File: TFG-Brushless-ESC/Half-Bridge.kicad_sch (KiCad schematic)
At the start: 9 parts, among them Q5 IRF1310, Q6 IRF1310, U5 IR2101

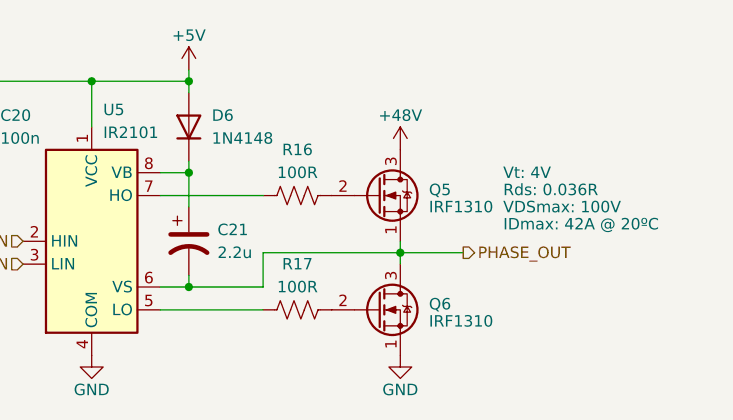
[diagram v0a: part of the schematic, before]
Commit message: Changes in half-bridge
Corrected voltage from 48 to 24V and 5V Vcc to 12V Vcc
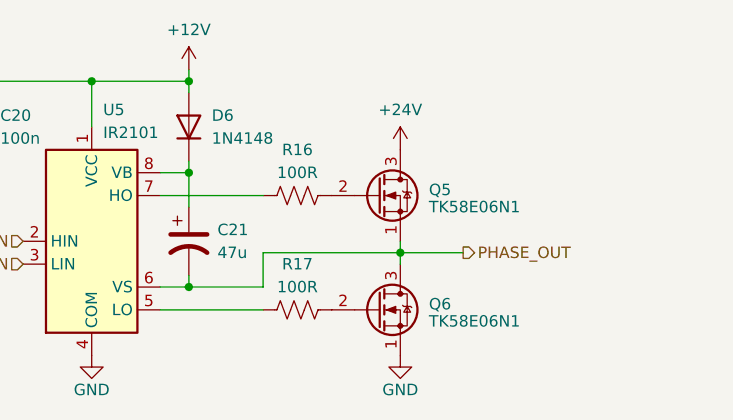
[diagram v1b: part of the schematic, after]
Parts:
- C21: value 2.2u -> 47u
- Q5, Q6: value IRF1310 -> TK58E06N1
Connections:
- net +48V renamed +24V
- net +5V renamed +12V
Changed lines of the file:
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@@
 		)
 		(instances
-			(project "RTSpeed"
+			(project "TFG-Brushless-ESC"
 				(path "/fc8dd9a9-f99a-4338-8182-2c8b4b8ed6dd/b5458e57-2ddd-4d30-9620-d640c1a391c8"
 					(reference "#PWR042")
@@
 		)
 		(instances
-			(project "RTSpeed"
+			(project "TFG-Brushless-ESC"
 				(path "/fc8dd9a9-f99a-4338-8182-2c8b4b8ed6dd/b5458e57-2ddd-4d30-9620-d640c1a391c8"
 					(reference "C22")
@@
 		)
 		(instances
-			(project "RTSpeed"
+			(project "TFG-Brushless-ESC"
 				(path "/fc8dd9a9-f99a-4338-8182-2c8b4b8ed6dd/211b6883-96c8-42a2-bec5-a4dfd4e56ba6"
 					(reference "R17")
@@
 				(path "/fc8dd9a9-f99a-4338-8182-2c8b4b8ed6dd/f6e668ab-a50d-4861-bee8-58a57ed6fcc7"
 					(reference "R15")
+					(unit 1)
+				)
+			)
+		)
+	)
+	(symbol
+		(lib_id "power:+24V")
+		(at 96.52 78.105 0)
+		(unit 1)
+		(exclude_from_sim no)
+		(in_bom yes)
+		(on_board yes)
+		(dnp no)
+		(fields_autoplaced yes)
+		(property "Reference" "#PWR041"
+			(at 96.52 81.915 0)
+			(effects
+				(font
+					(size 1.27 1.27)
+				)
+				(hide yes)
+			)
+		)
+		(property "Value" "+24V"
+			(at 96.52 73.66 0)
+			(effects
+				(font
+					(size 1.27 1.27)
+				)
+			)
+		)
+		(property "Footprint" ""
+			(at 96.52 78.105 0)
+			(effects
+				(font
+					(size 1.27 1.27)
+				)
+				(hide yes)
+			)
+		)
+		(property "Datasheet" ""
+			(at 96.52 78.105 0)
+			(effects
+				(font
+					(size 1.27 1.27)
+				)
+				(hide yes)
+			)
+		)
+		(property "Description" "Power symbol creates a global label with name \"+24V\""
+			(at 96.52 78.105 0)
+			(effects
+				(font
+					(size 1.27 1.27)
+				)
+				(hide yes)
+			)
+		)
+		(pin "1"
+		)
+		(instances
+			(project "TFG-Brushless-ESC"
+				(path "/fc8dd9a9-f99a-4338-8182-2c8b4b8ed6dd/b5458e57-2ddd-4d30-9620-d640c1a391c8"
+					(reference "#PWR041")
+					(unit 1)
+				)
+				(path "/fc8dd9a9-f99a-4338-8182-2c8b4b8ed6dd/f6e668ab-a50d-4861-bee8-58a57ed6fcc7"
+					(reference "#PWR046")
+					(unit 1)
+				)
+				(path "/fc8dd9a9-f99a-4338-8182-2c8b4b8ed6dd/211b6883-96c8-42a2-bec5-a4dfd4e56ba6"
+					(reference "#PWR051")
 					(unit 1)
 				)
@@
 			)
 		)
-		(property "Value" "IRF1310"
+		(property "Value" "TK58E06N1"
 			(at 99.695 84.455 0)
 			(effects
@@
 				)
 				(justify left)
+				(hide yes)
 			)
 		)
@@
 				)
 				(justify left)
+				(hide yes)
 			)
 		)
@@
 				)
 				(justify left)
+				(hide yes)
 			)
 		)
@@
 				)
 				(justify left)
+				(hide yes)
 			)
 		)
@@
 		)
 		(instances
-			(project "RTSpeed"
+			(project "TFG-Brushless-ESC"
 				(path "/fc8dd9a9-f99a-4338-8182-2c8b4b8ed6dd/211b6883-96c8-42a2-bec5-a4dfd4e56ba6"
 					(reference "Q5")
@@
 		)
 		(instances
-			(project "RTSpeed"
+			(project "TFG-Brushless-ESC"
 				(path "/fc8dd9a9-f99a-4338-8182-2c8b4b8ed6dd/211b6883-96c8-42a2-bec5-a4dfd4e56ba6"
 					(reference "D6")
@@
 		)
 		(instances
-			(project "RTSpeed"
+			(project "TFG-Brushless-ESC"
 				(path "/fc8dd9a9-f99a-4338-8182-2c8b4b8ed6dd/b5458e57-2ddd-4d30-9620-d640c1a391c8"
 					(reference "#PWR055")
@@
 		)
 		(instances
-			(project "RTSpeed"
+			(project "TFG-Brushless-ESC"
 				(path "/fc8dd9a9-f99a-4338-8182-2c8b4b8ed6dd/211b6883-96c8-42a2-bec5-a4dfd4e56ba6"
 					(reference "U5")
@@
 		)
 		(instances
-			(project "RTSpeed"
+			(project "TFG-Brushless-ESC"
 				(path "/fc8dd9a9-f99a-4338-8182-2c8b4b8ed6dd/b5458e57-2ddd-4d30-9620-d640c1a391c8"
 					(reference "#PWR044")
@@
 		)
 		(instances
-			(project "RTSpeed"
+			(project "TFG-Brushless-ESC"
 				(path "/fc8dd9a9-f99a-4338-8182-2c8b4b8ed6dd/211b6883-96c8-42a2-bec5-a4dfd4e56ba6"
 					(reference "R16")
@@
 		)
 		(instances
-			(project "RTSpeed"
+			(project "TFG-Brushless-ESC"
 				(path "/fc8dd9a9-f99a-4338-8182-2c8b4b8ed6dd/211b6883-96c8-42a2-bec5-a4dfd4e56ba6"
 					(reference "C20")
@@
 			)
 		)
-		(property "Value" "IRF1310"
+		(property "Value" "TK58E06N1"
 			(at 99.695 97.1549 0)
 			(effects
@@
 		)
 		(instances
-			(project "RTSpeed"
+			(project "TFG-Brushless-ESC"
 				(path "/fc8dd9a9-f99a-4338-8182-2c8b4b8ed6dd/211b6883-96c8-42a2-bec5-a4dfd4e56ba6"
 					(reference "Q6")
@@
 		)
 		(instances
-			(project "RTSpeed"
+			(project "TFG-Brushless-ESC"
 				(path "/fc8dd9a9-f99a-4338-8182-2c8b4b8ed6dd/b5458e57-2ddd-4d30-9620-d640c1a391c8"
 					(reference "#PWR043")
@@
 				(path "/fc8dd9a9-f99a-4338-8182-2c8b4b8ed6dd/211b6883-96c8-42a2-bec5-a4dfd4e56ba6"
 					(reference "#PWR053")
-					(unit 1)
-				)
-			)
-		)
-	)
-	(symbol
-		(lib_id "power:+48V")
-		(at 96.52 78.105 0)
-		(unit 1)
-		(exclude_from_sim no)
-		(in_bom yes)
-		(on_board yes)
-		(dnp no)
-		(property "Reference" "#PWR041"
-			(at 96.52 81.915 0)
-			(effects
-				(font
-					(size 1.27 1.27)
-				)
-				(hide yes)
-			)
-		)
-		(property "Value" "+48V"
-			(at 96.52 74.295 0)
-			(effects
-				(font
-					(size 1.27 1.27)
-				)
-			)
-		)
-		(property "Footprint" ""
-			(at 96.52 78.105 0)
-			(effects
-				(font
-					(size 1.27 1.27)
-				)
-				(hide yes)
-			)
-		)
-		(property "Datasheet" ""
-			(at 96.52 78.105 0)
-			(effects
-				(font
-					(size 1.27 1.27)
-				)
-				(hide yes)
-			)
-		)
-		(property "Description" ""
-			(at 96.52 78.105 0)
-			(effects
-				(font
-					(size 1.27 1.27)
-				)
-				(hide yes)
-			)
-		)
-		(pin "1"
-		)
-		(instances
-			(project "RTSpeed"
-				(path "/fc8dd9a9-f99a-4338-8182-2c8b4b8ed6dd/b5458e57-2ddd-4d30-9620-d640c1a391c8"
-					(reference "#PWR041")
-					(unit 1)
-				)
-				(path "/fc8dd9a9-f99a-4338-8182-2c8b4b8ed6dd/f6e668ab-a50d-4861-bee8-58a57ed6fcc7"
-					(reference "#PWR046")
-					(unit 1)
-				)
-				(path "/fc8dd9a9-f99a-4338-8182-2c8b4b8ed6dd/211b6883-96c8-42a2-bec5-a4dfd4e56ba6"
-					(reference "#PWR051")
 					(unit 1)
 				)
@@
 			)
 		)
-		(property "Value" "2.2u"
+		(property "Value" "47u"
 			(at 76.2 89.535 0)
 			(effects
@@
 		)
 		(instances
-			(project "RTSpeed"
+			(project "TFG-Brushless-ESC"
 				(path "/fc8dd9a9-f99a-4338-8182-2c8b4b8ed6dd/211b6883-96c8-42a2-bec5-a4dfd4e56ba6"
 					(reference "C21")
@@
 	)
 	(symbol
-		(lib_id "power:+5V")
+		(lib_id "power:+12V")
 		(at 73.025 69.215 0)
 		(unit 1)
@@
 		(on_board yes)
 		(dnp no)
+		(fields_autoplaced yes)
 		(property "Reference" "#PWR040"
 			(at 73.025 73.025 0)
@@
 			)
 		)
-		(property "Value" "+5V"
-			(at 73.025 65.405 0)
+		(property "Value" "+12V"
+			(at 73.025 64.77 0)
 			(effects
 				(font
@@
 			)
 		)
-		(property "Description" ""
+		(property "Description" "Power symbol creates a global label with name \"+12V\""
 			(at 73.025 69.215 0)
 			(effects
@@
 		)
 		(instances
-			(project "RTSpeed"
+			(project "TFG-Brushless-ESC"
 				(path "/fc8dd9a9-f99a-4338-8182-2c8b4b8ed6dd/b5458e57-2ddd-4d30-9620-d640c1a391c8"
 					(reference "#PWR040")

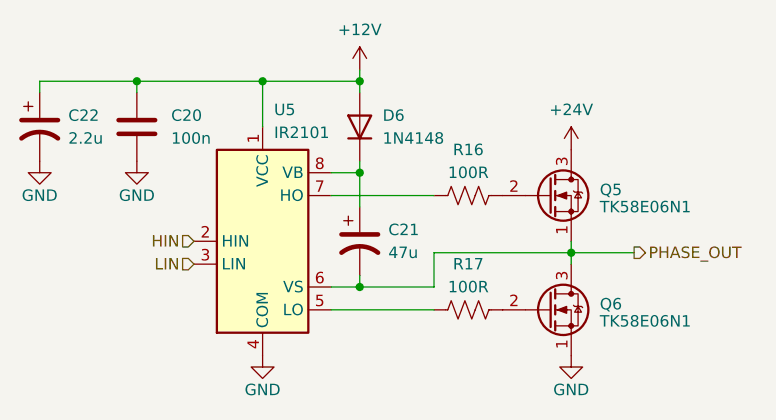
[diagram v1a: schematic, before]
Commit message: Attempt at implementing regenerative braking
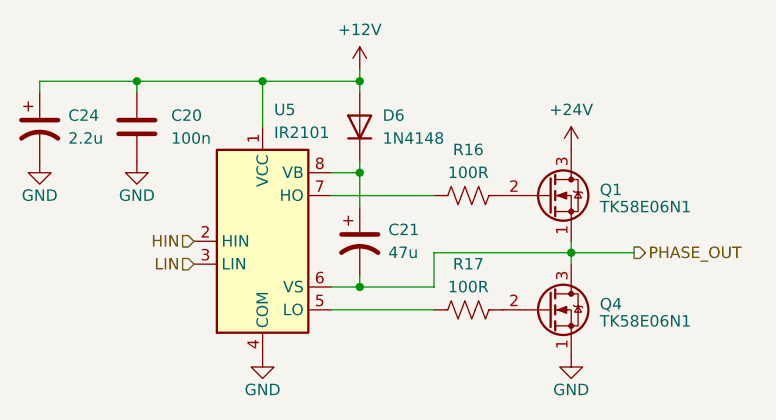
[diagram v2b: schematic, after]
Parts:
- removed Q5, Q6: TK58E06N1, Package_TO_SOT_THT:TO-92_Inline, symbol Transistor_FET:2N7000
- added Q1, Q4: TK58E06N1, Package_TO_SOT_THT:TO-220-3_Horizontal_TabDown, symbol Transistor_FET:2N7000
- renumbered C22 to C24
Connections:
- net +24V: now also Q1.3 (D)
- net GND: now also Q4.1 (S)
- net PHASE_OUT: now also Q1.1 (S), Q4.3 (D)
- net at R17.2: now also Q4.2 (G)
- net at R16.2: now also Q1.2 (G)
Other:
- company: (none) -> Adrián Teixeira de Uña

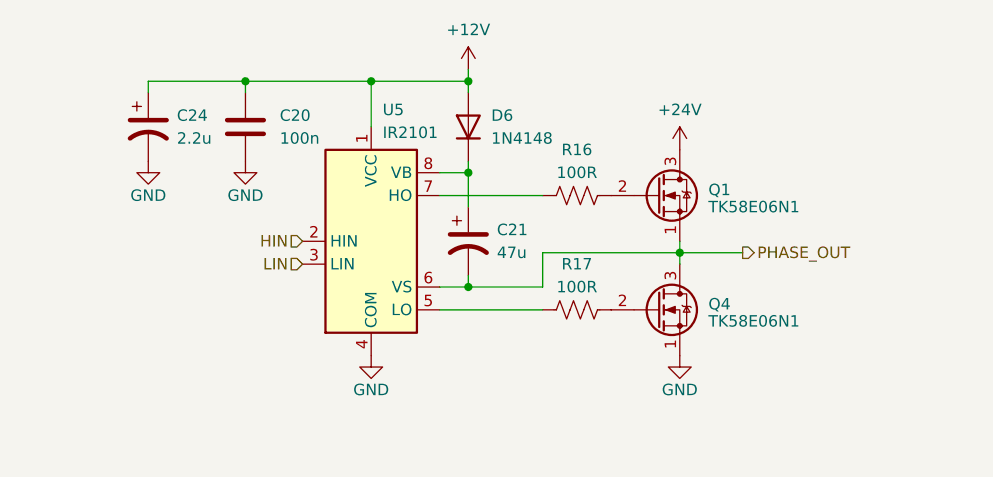
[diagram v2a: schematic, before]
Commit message: Figured out regenerative braking
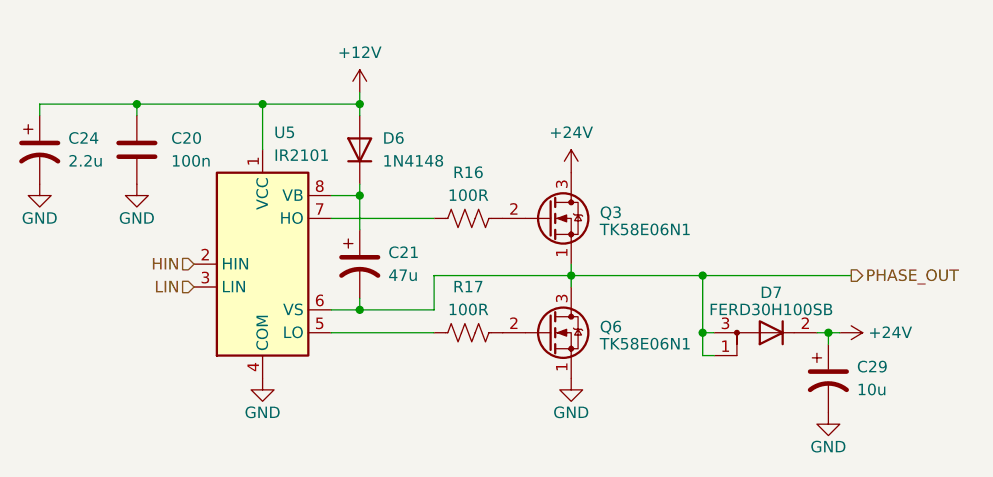
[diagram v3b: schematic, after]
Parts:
- added C29: 10u, Capacitor_THT:CP_Radial_D5.0mm_P2.00mm, symbol Device:C_Polarized_US
- added D7: FERD30H100SB, Package_TO_SOT_SMD:TO-252-2, symbol TFG-Brushless-ESC:D_AKA
- renumbered Q1 to Q3, Q4 to Q6
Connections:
- net +24V: now also C29.1, D7.2
- net GND: now also C29.2
- net PHASE_OUT: now also D7.1, D7.3
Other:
- moved on the sheet: C20, C21, C24, D6, Q3, Q6, R16, R17, U5

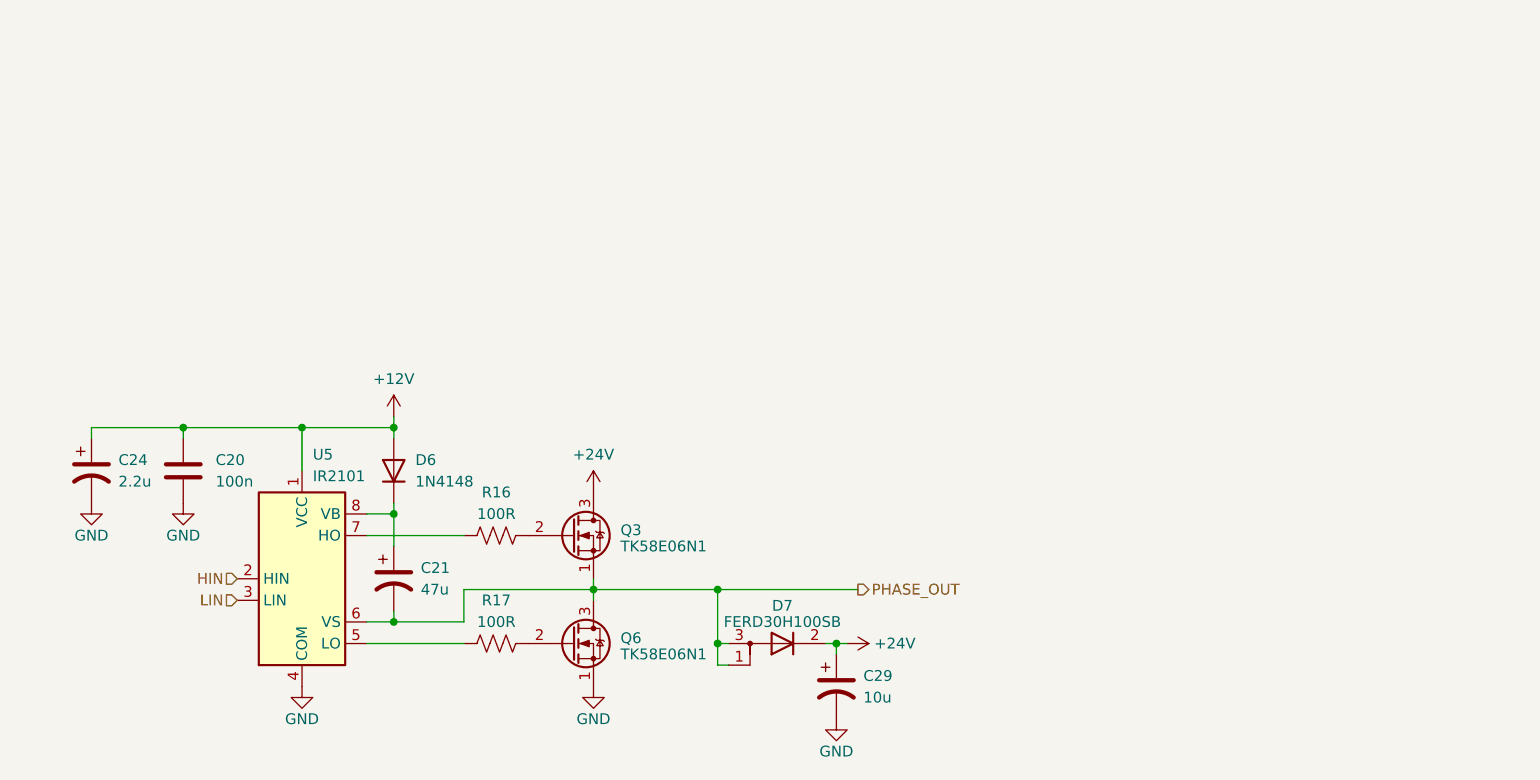
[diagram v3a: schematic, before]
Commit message: Added current and voltage sensing
Other changes: removed BAT Diode since it will not be used, renamed pins of STM32
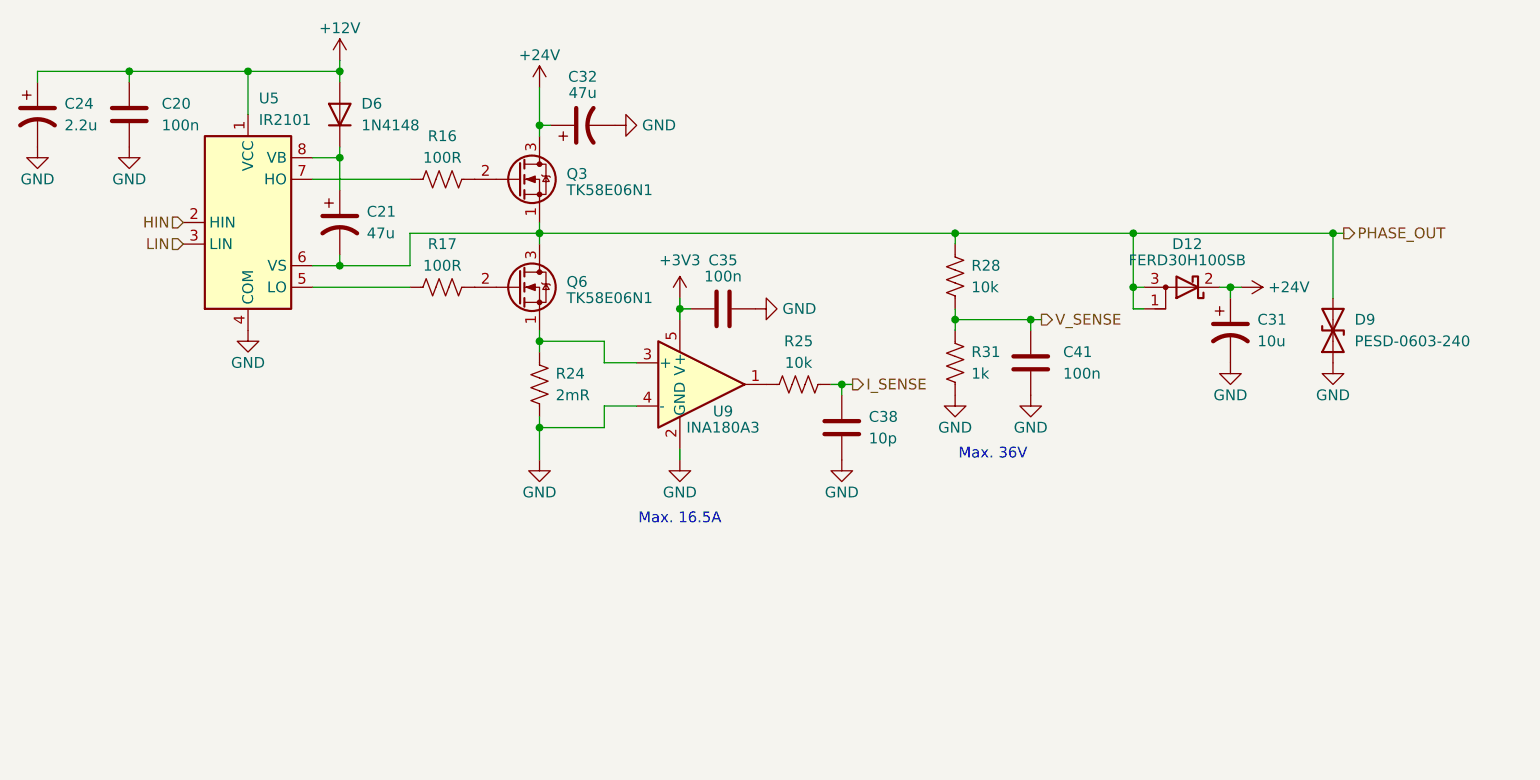
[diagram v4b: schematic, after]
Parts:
- removed D7: FERD30H100SB, Package_TO_SOT_SMD:TO-252-2, symbol TFG-Brushless-ESC:D_AKA
- added C32: 47u, Capacitor_THT:CP_Radial_D5.0mm_P2.00mm, symbol Device:C_Polarized_US
- added C35, C41: 100n, Capacitor_SMD:C_0603_1608Metric, symbol Device:C
- added C38: 10p, Capacitor_SMD:C_0603_1608Metric, symbol Device:C
- added D12: FERD30H100SB, Package_TO_SOT_SMD:TO-252-2, symbol Device:D_Schottky_AKA
- added D9: PESD-0603-240, symbol Device:D_TVS
- added R24: 2mR, symbol Device:R_US
- added R25, R28: 10k, Resistor_SMD:R_0603_1608Metric, symbol Device:R_US
- added R31: 1k, Resistor_SMD:R_0603_1608Metric, symbol Device:R_US
- added U9: INA180A3, Package_TO_SOT_SMD:SOT-23-5, symbol Amplifier_Current:INA180A3
- renumbered C29 to C31
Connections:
- net +24V: now also C32.1, D12.2 (K)
- net GND: now also C32.2, C35.2, C38.1, C41.2, D9.1 (A1), R24.2, R31.1, U9.2 (GND), U9.4 (-); no longer Q6.1 (S)
- net PHASE_OUT: now also D12.1 (A), D12.3 (A), D9.2 (A2), R28.2
- new net: Q6.1 (S), R24.1, U9.3 (+)
- new net: R25.1, U9.1
- new net +3V3: C35.1, U9.5 (V+)
- new net I_SENSE: C38.2, R25.2
- new net V_SENSE: C41.1, R28.1, R31.2
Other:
- note added: "Max. 16.5A"
- note added: "Max. 36V"
- moved on the sheet: C20, C21, C24, C31, D6, Q3, Q6, R16, R17, U5

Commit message: STM and Eeschema changes
STM tests and fixed MOSFET error in Half Bridge
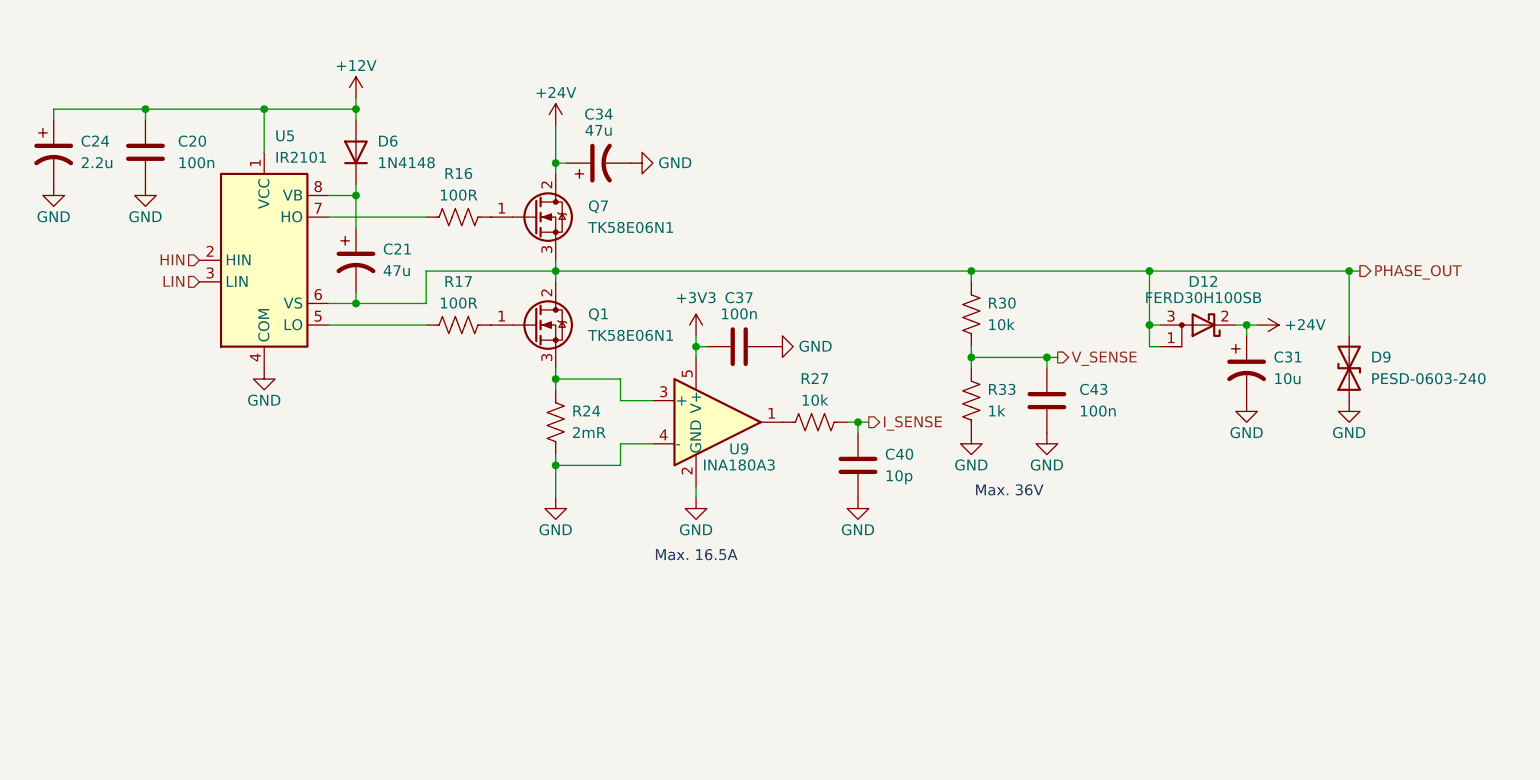
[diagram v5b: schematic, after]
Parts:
- removed Q3, Q6: TK58E06N1, Package_TO_SOT_THT:TO-220-3_Horizontal_TabDown, symbol Transistor_FET:2N7000
- added Q1, Q7: TK58E06N1, Package_TO_SOT_THT:TO-220-3_Vertical, symbol Device:Q_NMOS_GDS
- U5: footprint Package_DIP:DIP-8_W10.16mm -> Package_SO:SOIC-8-1EP_3.9x4.9mm_P1.27mm_EP2.29x3mm
- renumbered C32 to C34, C35 to C37, C38 to C40, C41 to C43, R25 to R27, R28 to R30, R31 to R33
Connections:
- net +24V: now also Q7.2 (D)
- net PHASE_OUT: now also Q1.2 (D), Q7.3 (S)
- net at R17.2: now also Q1.1 (G)
- net at R16.2: now also Q7.1 (G)
- net at R24.1, U9.3 (+): now also Q1.3 (S)
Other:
- moved on the sheet: C20, C21, C24, C31, C34, C37, C40, C43, D12, D6, D9, R16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
